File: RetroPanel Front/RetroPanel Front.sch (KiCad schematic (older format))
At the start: 11 parts, among them J1 Front Panel, M1 Mounting_Pin, M2 Mounting_Pin, M3 Mounting_Pin, M4 Mounting_Pin, SW1 TURBO, SW2 POWER, SW3 RESET, U1 3641AH

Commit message: Layout first draft
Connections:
- net 7S_A: now also J1.11 (7S_A); no longer J1.4 (SW_PWR1)
- net 7S_B: now also J1.21 (7S_B); no longer J1.5 (SW_PWR2)
- net 7S_C: now also J1.16 (7S_C); no longer J1.6 (LED_PWR1)
- net 7S_D: now also J1.14 (7S_D); no longer J1.7 (LED_PWR2)
- net 7S_D1: now also J1.10 (7S_D1); no longer J1.12 (7S_F)
- net 7S_D2: now also J1.19 (7S_D2); no longer J1.13 (7S_E)
- net 7S_D3: now also J1.20 (7S_D3); no longer J1.14 (7S_D)
- net 7S_D4: now also J1.18 (7S_D4); no longer J1.15 (7S_DP)
- net 7S_DP: now also J1.15 (7S_DP); no longer J1.11 (7S_A)
- net 7S_E: now also J1.13 (7S_E); no longer J1.8 (SW_RESET1)
- net 7S_F: now also J1.12 (7S_F); no longer J1.9 (SW_RESET2)
- net 7S_G: now also J1.17 (7S_G); no longer J1.10 (7S_D1)
- net LED_PWR1: now also J1.6 (LED_PWR1); no longer J1.18 (7S_D4)
- net LED_PWR2: now also J1.7 (LED_PWR2); no longer J1.19 (7S_D2)
- net LED_TURBO1: now also J1.24 (SW_EXTRA1); no longer J1.22 (LED_HDD1)
- net LED_TURBO2: now also J1.25 (SW_EXTRA2); no longer J1.23 (LED_HDD2)
- net SW_PWR1: now also J1.4 (SW_PWR1); no longer J1.16 (7S_C)
- net SW_PWR2: now also J1.5 (SW_PWR2); no longer J1.17 (7S_G)
- net SW_TURBO1: now also J1.22 (LED_HDD1); no longer J1.20 (7S_D3)
- net SW_TURBO2: now also J1.23 (LED_HDD2); no longer J1.21 (7S_B)
- net SW_RES1 renamed SW_RESET1
- net SW_RESET1: now also J1.8 (SW_RESET1); no longer J1.24 (SW_EXTRA1)
- net SW_RES2 renamed SW_RESET2
- net SW_RESET2: now also J1.9 (SW_RESET2); no longer J1.25 (SW_EXTRA2)
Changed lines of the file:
@@
 $EndComp
 Text GLabel 1375 6150 0    50   Output ~ 0
-SW_RES1
+SW_RESET1
 NoConn ~ 1925 6050
 Wire Wire Line
@@
 	2000 6250 1925 6250
 Text GLabel 2075 6900 2    50   Output ~ 0
-SW_RES2
+SW_RESET2
 Wire Wire Line
 	2000 6900 2075 6900
@@
 Wire Bus Line
 	4800 2775 7800 2775
-Text Label 8775 3225 0    50   ~ 0
-7S_A
-Text Label 8775 3325 0    50   ~ 0
-7S_B
-Text Label 8775 3425 0    50   ~ 0
-7S_C
-Text Label 8775 3525 0    50   ~ 0
-7S_D
-Text Label 8775 3625 0    50   ~ 0
-7S_E
-Text Label 8775 3725 0    50   ~ 0
-7S_F
-Text Label 8775 3825 0    50   ~ 0
-7S_G
-Text Label 8775 3925 0    50   ~ 0
-7S_DP
-Wire Wire Line
-	8750 3225 9050 3225
-Wire Wire Line
-	8750 3325 9050 3325
-Wire Wire Line
-	8750 3425 9050 3425
-Wire Wire Line
-	8750 3525 9050 3525
-Wire Wire Line
-	8750 3625 9050 3625
-Wire Wire Line
-	8750 3725 9050 3725
-Wire Wire Line
-	8750 3825 9050 3825
-Wire Wire Line
-	8750 3925 9050 3925
-Text Label 8775 4025 0    50   ~ 0
-7S_D1
-Text Label 8775 4125 0    50   ~ 0
-7S_D2
-Text Label 8775 4225 0    50   ~ 0
-7S_D3
-Text Label 8775 4325 0    50   ~ 0
-7S_D4
-Wire Wire Line
-	9050 4025 8750 4025
-Wire Wire Line
-	9050 4125 8750 4125
-Wire Wire Line
-	9050 4225 8750 4225
-Wire Wire Line
-	9050 4325 8750 4325
 Wire Wire Line
 	9050 5425 8975 5425
@@
 Wire Wire Line
 	8975 5425 8975 5500
-Text GLabel 8750 4425 0    50   Input ~ 0
+Text GLabel 8975 3225 0    50   Input ~ 0
 SW_PWR1
-Text GLabel 8750 4525 0    50   Input ~ 0
+Text GLabel 8975 3325 0    50   Input ~ 0
 SW_PWR2
-Text GLabel 8750 4625 0    50   Output ~ 0
+Text GLabel 8975 3425 0    50   Output ~ 0
 LED_PWR1
-Text GLabel 8750 4725 0    50   Input ~ 0
+Text GLabel 8975 3525 0    50   Input ~ 0
 LED_PWR2
-Text GLabel 8750 4825 0    50   Input ~ 0
+Text GLabel 8975 5025 0    50   Input ~ 0
 SW_TURBO1
-Text GLabel 8750 4925 0    50   Input ~ 0
+Text GLabel 8975 5125 0    50   Input ~ 0
 SW_TURBO2
-Text GLabel 8750 5025 0    50   Output ~ 0
+Text GLabel 8975 5225 0    50   Output ~ 0
 LED_TURBO1
-Text GLabel 8750 5125 0    50   Input ~ 0
+Text GLabel 8975 5325 0    50   Input ~ 0
 LED_TURBO2
-Text GLabel 8750 5225 0    50   Input ~ 0
-SW_RES1
-Text GLabel 8750 5325 0    50   Input ~ 0
-SW_RES2
-Wire Wire Line
-	8750 4425 9050 4425
-Wire Wire Line
-	8750 4525 9050 4525
-Wire Wire Line
-	8750 4625 9050 4625
-Wire Wire Line
-	8750 4725 9050 4725
-Wire Wire Line
-	8750 4825 9050 4825
-Wire Wire Line
-	8750 4925 9050 4925
-Wire Wire Line
-	8750 5025 9050 5025
-Wire Wire Line
-	8750 5125 9050 5125
-Wire Wire Line
-	8750 5225 9050 5225
-Wire Wire Line
-	8750 5325 9050 5325
+Text GLabel 8975 3625 0    50   Input ~ 0
+SW_RESET1
+Text GLabel 8975 3725 0    50   Input ~ 0
+SW_RESET2
 $Comp
 L power:PWR_FLAG #FLG0101
@@
 $EndComp
 Entry Wire Line
-	8750 3625 8650 3525
-Entry Wire Line
-	8750 3725 8650 3625
-Entry Wire Line
-	8750 3825 8650 3725
-Entry Wire Line
-	8750 3925 8650 3825
-Entry Wire Line
-	8750 4025 8650 3925
-Entry Wire Line
-	8750 4125 8650 4025
-Entry Wire Line
-	8750 4225 8650 4125
-Entry Wire Line
-	8750 4325 8650 4225
-Entry Wire Line
-	8750 3225 8650 3125
-Entry Wire Line
-	8750 3325 8650 3225
-Entry Wire Line
-	8750 3425 8650 3325
-Entry Wire Line
-	8750 3525 8650 3425
+	8200 4225 8100 4125
+Entry Wire Line
+	8200 4325 8100 4225
+Entry Wire Line
+	8200 4425 8100 4325
+Entry Wire Line
+	8200 4525 8100 4425
+Entry Wire Line
+	8200 4625 8100 4525
+Entry Wire Line
+	8200 4725 8100 4625
+Entry Wire Line
+	8200 4825 8100 4725
+Entry Wire Line
+	8200 4925 8100 4825
+Entry Wire Line
+	8200 3825 8100 3725
+Entry Wire Line
+	8200 3925 8100 3825
+Entry Wire Line
+	8200 4025 8100 3925
+Entry Wire Line
+	8200 4125 8100 4025
 Connection ~ 8975 3125
-Wire Bus Line
-	8650 2775 7800 2775
+Connection ~ 7800 2775
+Wire Wire Line
+	8975 3225 9050 3225
+Wire Wire Line
+	8975 3325 9050 3325
+Wire Wire Line
+	8975 3425 9050 3425
+Wire Wire Line
+	8975 3525 9050 3525
+Wire Wire Line
+	8975 3625 9050 3625
+Wire Wire Line
+	8975 3725 9050 3725
+Wire Wire Line
+	8975 5025 9050 5025
+Wire Wire Line
+	8975 5125 9050 5125
+Wire Wire Line
+	8975 5225 9050 5225
+Wire Wire Line
+	8975 5325 9050 5325
+Wire Wire Line
+	8200 3825 9050 3825
+Wire Bus Line
+	8100 2775 7800 2775
+Text Label 8225 3825 0    50   ~ 0
+7S_D1
+Text Label 8225 4925 0    50   ~ 0
+7S_B
+Text Label 8225 4425 0    50   ~ 0
+7S_C
+Text Label 8225 4225 0    50   ~ 0
+7S_D
+Text Label 8225 4525 0    50   ~ 0
+7S_G
+Text Label 8225 4325 0    50   ~ 0
+7S_DP
+Text Label 8225 4725 0    50   ~ 0
+7S_D2
+Text Label 8225 4825 0    50   ~ 0
+7S_D3
+Text Label 8225 4625 0    50   ~ 0
+7S_D4
+Wire Wire Line
+	8200 3925 9050 3925
+Wire Wire Line
+	8200 4025 9050 4025
+Wire Wire Line
+	8200 4125 9050 4125
+Wire Wire Line
+	8200 4225 9050 4225
+Wire Wire Line
+	8200 4325 9050 4325
+Wire Wire Line
+	8200 4425 9050 4425
+Wire Wire Line
+	8200 4525 9050 4525
+Wire Wire Line
+	8200 4625 9050 4625
+Wire Wire Line
+	8200 4725 9050 4725
+Wire Wire Line
+	8200 4825 9050 4825
+Wire Wire Line
+	8200 4925 9050 4925
 Wire Bus Line
 	7800 2275 7800 2775
@@
 	4800 1875 4800 2775
 Wire Bus Line
-	8650 2775 8650 4225
-Connection ~ 7800 2775
+	8100 2775 8100 4825
+Text Label 8225 3925 0    50   ~ 0
+7S_A
+Text Label 8225 4025 0    50   ~ 0
+7S_F
+Text Label 8225 4125 0    50   ~ 0
+7S_E
 $EndSCHEMATC

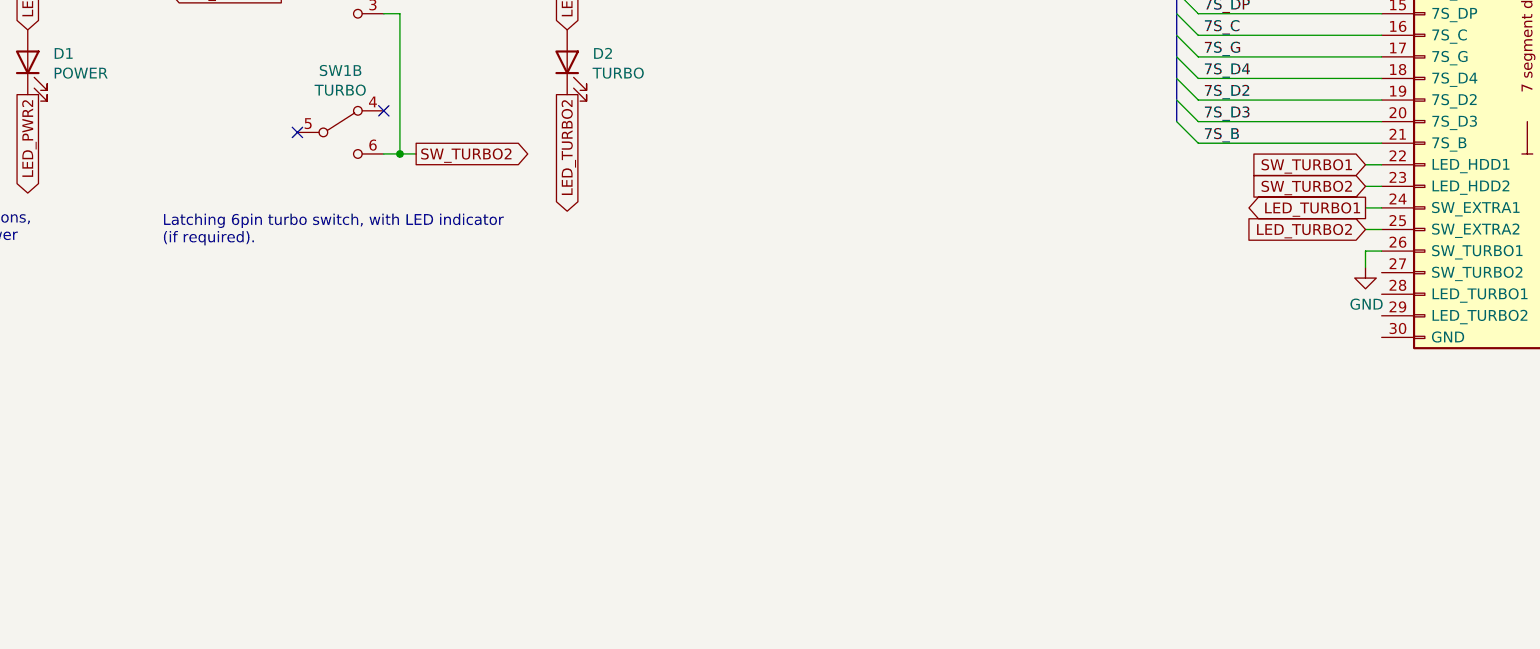
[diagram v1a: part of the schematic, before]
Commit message: Add extra switch and tweak size
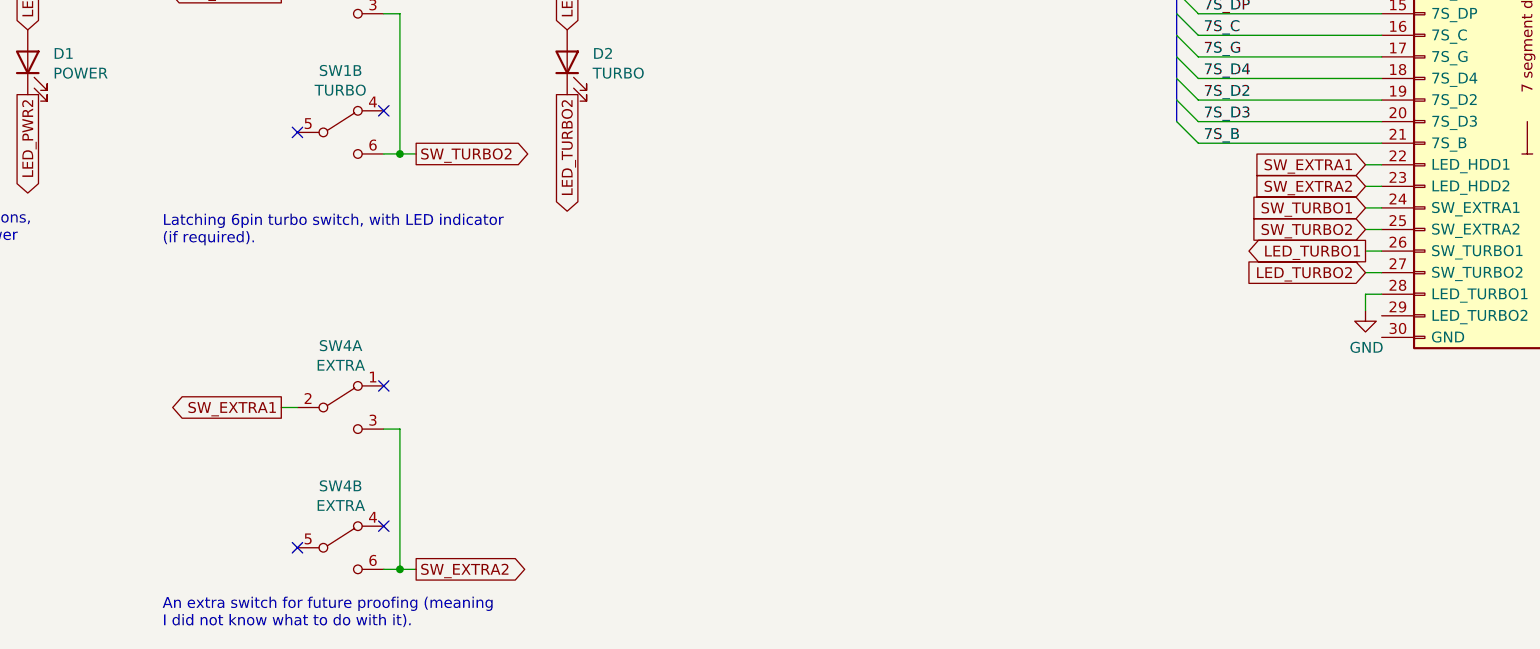
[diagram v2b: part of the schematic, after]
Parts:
- added SW4: EXTRA, 6pin_switch:dpdt_switch_black, symbol Switch:SW_DPDT_x2
- J1: footprint Connector_PinHeader_2.54mm:PinHeader_1x24_P2.54mm_Horizontal -> Connector_PinHeader_2.54mm:PinHeader_1x26_P2.54mm_Horizontal
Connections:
- net GND: now also J1.28 (LED_TURBO1); no longer J1.26 (SW_TURBO1)
- net LED_TURBO1: now also J1.26 (SW_TURBO1); no longer J1.24 (SW_EXTRA1)
- net LED_TURBO2: now also J1.27 (SW_TURBO2); no longer J1.25 (SW_EXTRA2)
- net SW_TURBO1: now also J1.24 (SW_EXTRA1); no longer J1.22 (LED_HDD1)
- net SW_TURBO2: now also J1.25 (SW_EXTRA2); no longer J1.23 (LED_HDD2)
- new net SW_EXTRA1: J1.22 (LED_HDD1), SW4.2 (B)
- new net SW_EXTRA2: J1.23 (LED_HDD2), SW4.3 (C), SW4.6 (C)
- no-connect marks 7 -> 10
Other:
- note added: "An extra switch for future proofing (meaning\nI did not know what to do with it)."
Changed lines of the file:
@@
 F 0 "J1" H 9200 5325 50  0000 L CNN
 F 1 "Front Panel" H 9200 5250 50  0000 L CNN
-F 2 "Connector_PinHeader_2.54mm:PinHeader_1x24_P2.54mm_Horizontal" H 9250 4125 50  0001 C CNN
+F 2 "Connector_PinHeader_2.54mm:PinHeader_1x26_P2.54mm_Horizontal" H 9250 4125 50  0001 C CNN
 F 3 "~" H 9250 4125 50  0001 C CNN
 	1    9250 4125
@@
 L power:GND #PWR0101
 U 1 1 6282785A
-P 8975 5500
-F 0 "#PWR0101" H 8975 5250 50  0001 C CNN
-F 1 "GND" H 8980 5327 50  0000 C CNN
-F 2 "" H 8975 5500 50  0001 C CNN
-F 3 "" H 8975 5500 50  0001 C CNN
-	1    8975 5500
+P 8975 5700
+F 0 "#PWR0101" H 8975 5450 50  0001 C CNN
+F 1 "GND" H 8980 5527 50  0000 C CNN
+F 2 "" H 8975 5700 50  0001 C CNN
+F 3 "" H 8975 5700 50  0001 C CNN
+	1    8975 5700
 	1    0    0    -1
 $EndComp
@@
 	4800 2775 7800 2775
 Wire Wire Line
-	9050 5425 8975 5425
+	9050 5625 8975 5625
 Wire Wire Line
 	8975 3050 8975 3125
@@
 	8975 3125 9050 3125
 Wire Wire Line
-	8975 5425 8975 5500
+	8975 5625 8975 5700
 Text GLabel 8975 3225 0    50   Input ~ 0
 SW_PWR1
@@
 Text GLabel 8975 3525 0    50   Input ~ 0
 LED_PWR2
-Text GLabel 8975 5025 0    50   Input ~ 0
+Text GLabel 8975 5225 0    50   Input ~ 0
 SW_TURBO1
-Text GLabel 8975 5125 0    50   Input ~ 0
+Text GLabel 8975 5325 0    50   Input ~ 0
 SW_TURBO2
-Text GLabel 8975 5225 0    50   Output ~ 0
+Text GLabel 8975 5425 0    50   Output ~ 0
 LED_TURBO1
-Text GLabel 8975 5325 0    50   Input ~ 0
+Text GLabel 8975 5525 0    50   Input ~ 0
 LED_TURBO2
 Text GLabel 8975 3625 0    50   Input ~ 0
@@
 	8975 3725 9050 3725
 Wire Wire Line
-	8975 5025 9050 5025
-Wire Wire Line
-	8975 5125 9050 5125
-Wire Wire Line
 	8975 5225 9050 5225
 Wire Wire Line
 	8975 5325 9050 5325
+Wire Wire Line
+	8975 5425 9050 5425
+Wire Wire Line
+	8975 5525 9050 5525
 Wire Wire Line
 	8200 3825 9050 3825
@@
 Wire Wire Line
 	8200 4925 9050 4925
+Text Label 8225 3925 0    50   ~ 0
+7S_A
+Text Label 8225 4025 0    50   ~ 0
+7S_F
+Text Label 8225 4125 0    50   ~ 0
+7S_E
+$Comp
+L Switch:SW_DPDT_x2 SW4
+U 1 1 6374F345
+P 4225 6150
+F 0 "SW4" H 4225 6435 50  0000 C CNN
+F 1 "EXTRA" H 4225 6344 50  0000 C CNN
+F 2 "6pin_switch:dpdt_switch_black" H 4225 6150 50  0001 C CNN
+F 3 "~" H 4225 6150 50  0001 C CNN
+	1    4225 6150
+	1    0    0    -1
+$EndComp
+$Comp
+L Switch:SW_DPDT_x2 SW4
+U 2 1 6374F34B
+P 4225 6800
+F 0 "SW4" H 4225 7085 50  0000 C CNN
+F 1 "EXTRA" H 4225 6994 50  0000 C CNN
+F 2 "6pin_switch:dpdt_switch_black" H 4225 6800 50  0001 C CNN
+F 3 "~" H 4225 6800 50  0001 C CNN
+	2    4225 6800
+	1    0    0    -1
+$EndComp
+Text GLabel 3950 6150 0    50   Output ~ 0
+SW_EXTRA1
+Wire Wire Line
+	3950 6150 4025 6150
+NoConn ~ 4425 6050
+NoConn ~ 4025 6800
+NoConn ~ 4425 6700
+Wire Wire Line
+	4425 6900 4500 6900
+Wire Wire Line
+	4500 6900 4500 6250
+Wire Wire Line
+	4500 6250 4425 6250
+Text GLabel 4575 6900 2    50   Output ~ 0
+SW_EXTRA2
+Wire Wire Line
+	4500 6900 4575 6900
+Connection ~ 4500 6900
+Text Notes 3400 7175 0    50   ~ 0
+An extra switch for future proofing (meaning\nI did not know what to do with it).
+Text GLabel 8975 5025 0    50   Input ~ 0
+SW_EXTRA1
+Text GLabel 8975 5125 0    50   Input ~ 0
+SW_EXTRA2
+Wire Wire Line
+	8975 5025 9050 5025
+Wire Wire Line
+	8975 5125 9050 5125
 Wire Bus Line
 	7800 2275 7800 2775
@@
 Wire Bus Line
 	8100 2775 8100 4825
-Text Label 8225 3925 0    50   ~ 0
-7S_A
-Text Label 8225 4025 0    50   ~ 0
-7S_F
-Text Label 8225 4125 0    50   ~ 0
-7S_E
 $EndSCHEMATC

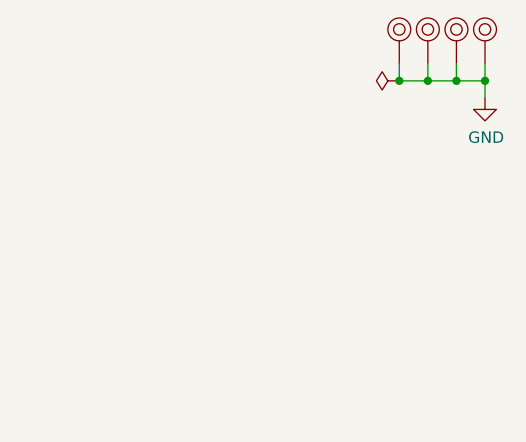
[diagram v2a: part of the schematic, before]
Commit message: Add mounting pads
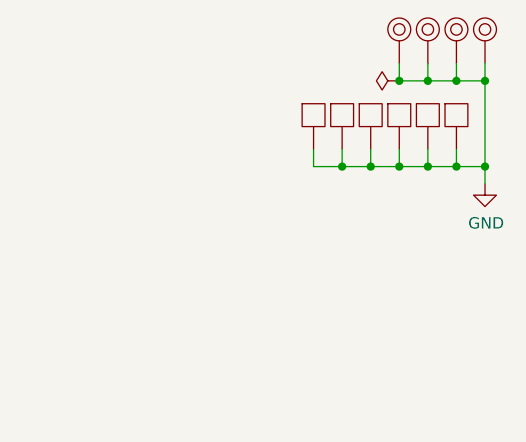
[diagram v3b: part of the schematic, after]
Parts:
- added M10, M5, M6, M7, M8, M9: Mounting_Pad, RetroPanel:Pad_pin, symbol mounting:Mounting_Pad
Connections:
- net GND: now also M10.1, M5.1, M6.1, M7.1, M8.1, M9.1
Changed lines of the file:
@@
 encoding utf-8
 Sheet 1 1
-Title "BulkyModem (Panel)"
+Title "BulkyModem (Front)"
 Date ""
 Rev "A"
@@
 L power:GND #PWR0111
 U 1 1 6282AADA
-P 11100 875
-F 0 "#PWR0111" H 11100 625 50  0001 C CNN
-F 1 "GND" H 11105 702 50  0000 C CNN
-F 2 "" H 11100 875 50  0001 C CNN
-F 3 "" H 11100 875 50  0001 C CNN
-	1    11100 875
+P 11100 1250
+F 0 "#PWR0111" H 11100 1000 50  0001 C CNN
+F 1 "GND" H 11105 1077 50  0000 C CNN
+F 2 "" H 11100 1250 50  0001 C CNN
+F 3 "" H 11100 1250 50  0001 C CNN
+	1    11100 1250
 	1    0    0    -1
 $EndComp
@@
 Wire Wire Line
 	10975 800  11100 800
-Wire Wire Line
-	11100 800  11100 875
 Connection ~ 11100 800
 $Comp
@@
 Wire Wire Line
 	8975 5125 9050 5125
+$Comp
+L mounting:Mounting_Pad M5
+U 1 1 637825FA
+P 10975 950
+F 0 "M5" H 10975 1050 50  0001 C CNN
+F 1 "Mounting_Pad" H 10975 875 50  0001 C CNN
+F 2 "RetroPanel:Pad_pin" H 10975 950 50  0001 C CNN
+F 3 "~" H 10975 950 50  0001 C CNN
+	1    10975 950
+	1    0    0    -1
+$EndComp
+Wire Wire Line
+	11100 800  11100 1175
+Connection ~ 11100 1175
+Wire Wire Line
+	11100 1175 11100 1250
+$Comp
+L mounting:Mounting_Pad M8
+U 1 1 6378DDBA
+P 10850 950
+F 0 "M8" H 10850 1050 50  0001 C CNN
+F 1 "Mounting_Pad" H 10850 875 50  0001 C CNN
+F 2 "RetroPanel:Pad_pin" H 10850 950 50  0001 C CNN
+F 3 "~" H 10850 950 50  0001 C CNN
+	1    10850 950
+	1    0    0    -1
+$EndComp
+$Comp
+L mounting:Mounting_Pad M7
+U 1 1 63790274
+P 10725 950
+F 0 "M7" H 10725 1050 50  0001 C CNN
+F 1 "Mounting_Pad" H 10725 875 50  0001 C CNN
+F 2 "RetroPanel:Pad_pin" H 10725 950 50  0001 C CNN
+F 3 "~" H 10725 950 50  0001 C CNN
+	1    10725 950
+	1    0    0    -1
+$EndComp
+$Comp
+L mounting:Mounting_Pad M6
+U 1 1 637928C6
+P 10600 950
+F 0 "M6" H 10600 1050 50  0001 C CNN
+F 1 "Mounting_Pad" H 10600 875 50  0001 C CNN
+F 2 "RetroPanel:Pad_pin" H 10600 950 50  0001 C CNN
+F 3 "~" H 10600 950 50  0001 C CNN
+	1    10600 950
+	1    0    0    -1
+$EndComp
+Wire Wire Line
+	10975 1100 10975 1175
+Connection ~ 10975 1175
+Wire Wire Line
+	10975 1175 11100 1175
+Wire Wire Line
+	10850 1100 10850 1175
+Connection ~ 10850 1175
+Wire Wire Line
+	10850 1175 10975 1175
+Wire Wire Line
+	10725 1100 10725 1175
+Connection ~ 10725 1175
+Wire Wire Line
+	10725 1175 10850 1175
+$Comp
+L mounting:Mounting_Pad M10
+U 1 1 637AD750
+P 10475 950
+F 0 "M10" H 10475 1050 50  0001 C CNN
+F 1 "Mounting_Pad" H 10475 875 50  0001 C CNN
+F 2 "RetroPanel:Pad_pin" H 10475 950 50  0001 C CNN
+F 3 "~" H 10475 950 50  0001 C CNN
+	1    10475 950
+	1    0    0    -1
+$EndComp
+$Comp
+L mounting:Mounting_Pad M9
+U 1 1 637AD756
+P 10350 950
+F 0 "M9" H 10350 1050 50  0001 C CNN
+F 1 "Mounting_Pad" H 10350 875 50  0001 C CNN
+F 2 "RetroPanel:Pad_pin" H 10350 950 50  0001 C CNN
+F 3 "~" H 10350 950 50  0001 C CNN
+	1    10350 950
+	1    0    0    -1
+$EndComp
+Wire Wire Line
+	10350 1100 10350 1175
+Wire Wire Line
+	10350 1175 10475 1175
+Wire Wire Line
+	10475 1100 10475 1175
+Connection ~ 10475 1175
+Wire Wire Line
+	10475 1175 10600 1175
+Wire Wire Line
+	10600 1100 10600 1175
+Connection ~ 10600 1175
+Wire Wire Line
+	10600 1175 10725 1175
 Wire Bus Line
 	7800 2275 7800 2775

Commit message: Rough layout of module
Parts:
- removed M6, M8: Mounting_Pad, RetroPanel:Pad_pin, symbol mounting:Mounting_Pad
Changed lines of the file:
@@
 encoding utf-8
 Sheet 1 1
-Title "BulkyModem (Front)"
+Title "RetroPanel (Front)"
 Date ""
 Rev "A"
@@
 Comment2 ""
 Comment3 ""
-Comment4 "Front panel for mounting LEDs horizontally, designed for slotting into the main module."
+Comment4 "3.5\" Front panel"
 $EndDescr
 $Comp
@@
 	11100 1175 11100 1250
 $Comp
-L mounting:Mounting_Pad M8
-U 1 1 6378DDBA
+L mounting:Mounting_Pad M7
+U 1 1 63790274
 P 10850 950
-F 0 "M8" H 10850 1050 50  0001 C CNN
+F 0 "M7" H 10850 1050 50  0001 C CNN
 F 1 "Mounting_Pad" H 10850 875 50  0001 C CNN
 F 2 "RetroPanel:Pad_pin" H 10850 950 50  0001 C CNN
@@
 	1    0    0    -1
 $EndComp
-$Comp
-L mounting:Mounting_Pad M7
-U 1 1 63790274
+Wire Wire Line
+	10975 1100 10975 1175
+Connection ~ 10975 1175
+Wire Wire Line
+	10975 1175 11100 1175
+Wire Wire Line
+	10850 1100 10850 1175
+$Comp
+L mounting:Mounting_Pad M10
+U 1 1 637AD750
 P 10725 950
-F 0 "M7" H 10725 1050 50  0001 C CNN
+F 0 "M10" H 10725 1050 50  0001 C CNN
 F 1 "Mounting_Pad" H 10725 875 50  0001 C CNN
 F 2 "RetroPanel:Pad_pin" H 10725 950 50  0001 C CNN
@@
 $EndComp
 $Comp
-L mounting:Mounting_Pad M6
-U 1 1 637928C6
+L mounting:Mounting_Pad M9
+U 1 1 637AD756
 P 10600 950
-F 0 "M6" H 10600 1050 50  0001 C CNN
+F 0 "M9" H 10600 1050 50  0001 C CNN
 F 1 "Mounting_Pad" H 10600 875 50  0001 C CNN
 F 2 "RetroPanel:Pad_pin" H 10600 950 50  0001 C CNN
@@
 $EndComp
 Wire Wire Line
-	10975 1100 10975 1175
-Connection ~ 10975 1175
-Wire Wire Line
-	10975 1175 11100 1175
-Wire Wire Line
-	10850 1100 10850 1175
+	10600 1100 10600 1175
+Wire Wire Line
+	10725 1100 10725 1175
 Connection ~ 10850 1175
 Wire Wire Line
 	10850 1175 10975 1175
 Wire Wire Line
-	10725 1100 10725 1175
+	10600 1175 10725 1175
 Connection ~ 10725 1175
 Wire Wire Line
 	10725 1175 10850 1175
-$Comp
-L mounting:Mounting_Pad M10
-U 1 1 637AD750
-P 10475 950
-F 0 "M10" H 10475 1050 50  0001 C CNN
-F 1 "Mounting_Pad" H 10475 875 50  0001 C CNN
-F 2 "RetroPanel:Pad_pin" H 10475 950 50  0001 C CNN
-F 3 "~" H 10475 950 50  0001 C CNN
-	1    10475 950
-	1    0    0    -1
-$EndComp
-$Comp
-L mounting:Mounting_Pad M9
-U 1 1 637AD756
-P 10350 950
-F 0 "M9" H 10350 1050 50  0001 C CNN
-F 1 "Mounting_Pad" H 10350 875 50  0001 C CNN
-F 2 "RetroPanel:Pad_pin" H 10350 950 50  0001 C CNN
-F 3 "~" H 10350 950 50  0001 C CNN
-	1    10350 950
-	1    0    0    -1
-$EndComp
-Wire Wire Line
-	10350 1100 10350 1175
-Wire Wire Line
-	10350 1175 10475 1175
-Wire Wire Line
-	10475 1100 10475 1175
-Connection ~ 10475 1175
-Wire Wire Line
-	10475 1175 10600 1175
-Wire Wire Line
-	10600 1100 10600 1175
-Connection ~ 10600 1175
-Wire Wire Line
-	10600 1175 10725 1175
 Wire Bus Line
 	7800 2275 7800 2775
